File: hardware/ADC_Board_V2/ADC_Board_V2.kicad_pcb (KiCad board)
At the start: 2 copper layers, 11 parts, among them J1 Pot 01, J2 Pot 02, J3 Pot 03, J4 Pot 04, J5 Pot 05, J6 Pot 06, J7 Pot 07, J8 Pot 08, J9 Data, U1 MCP3008

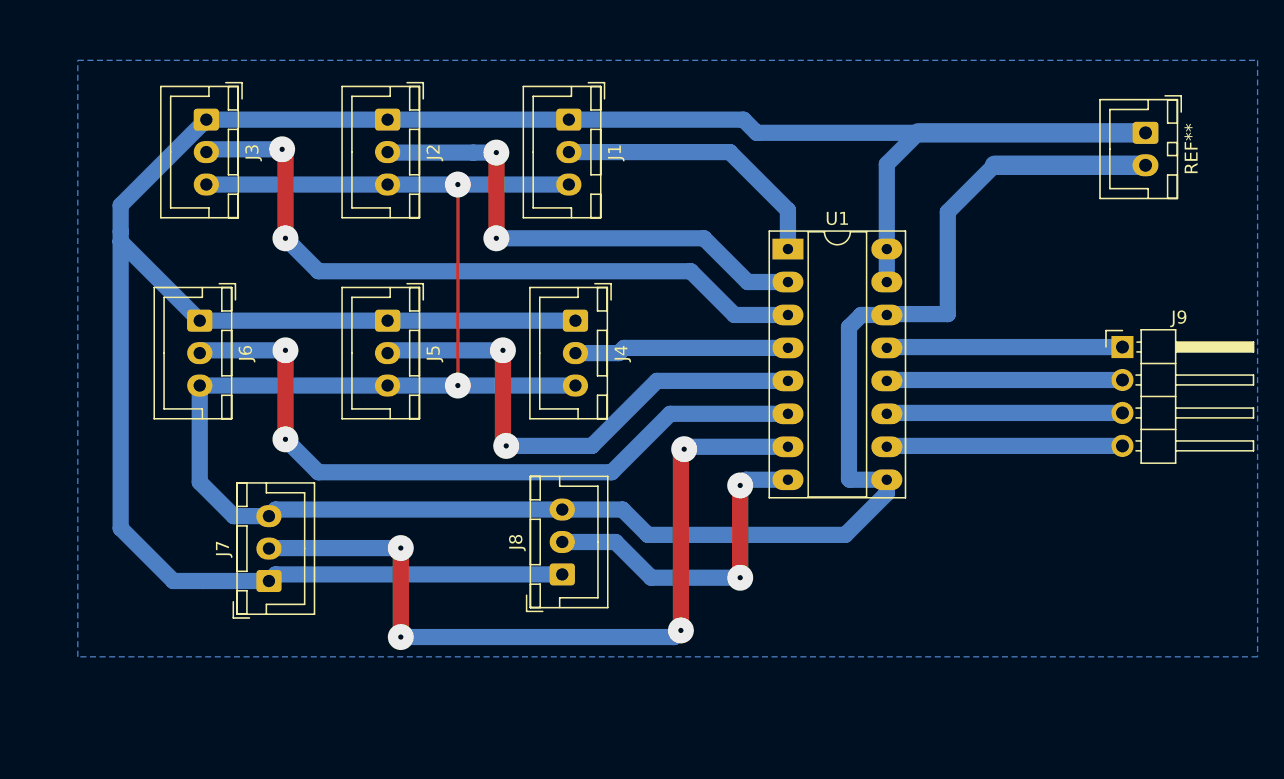
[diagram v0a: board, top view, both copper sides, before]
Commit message: updated ADC board design
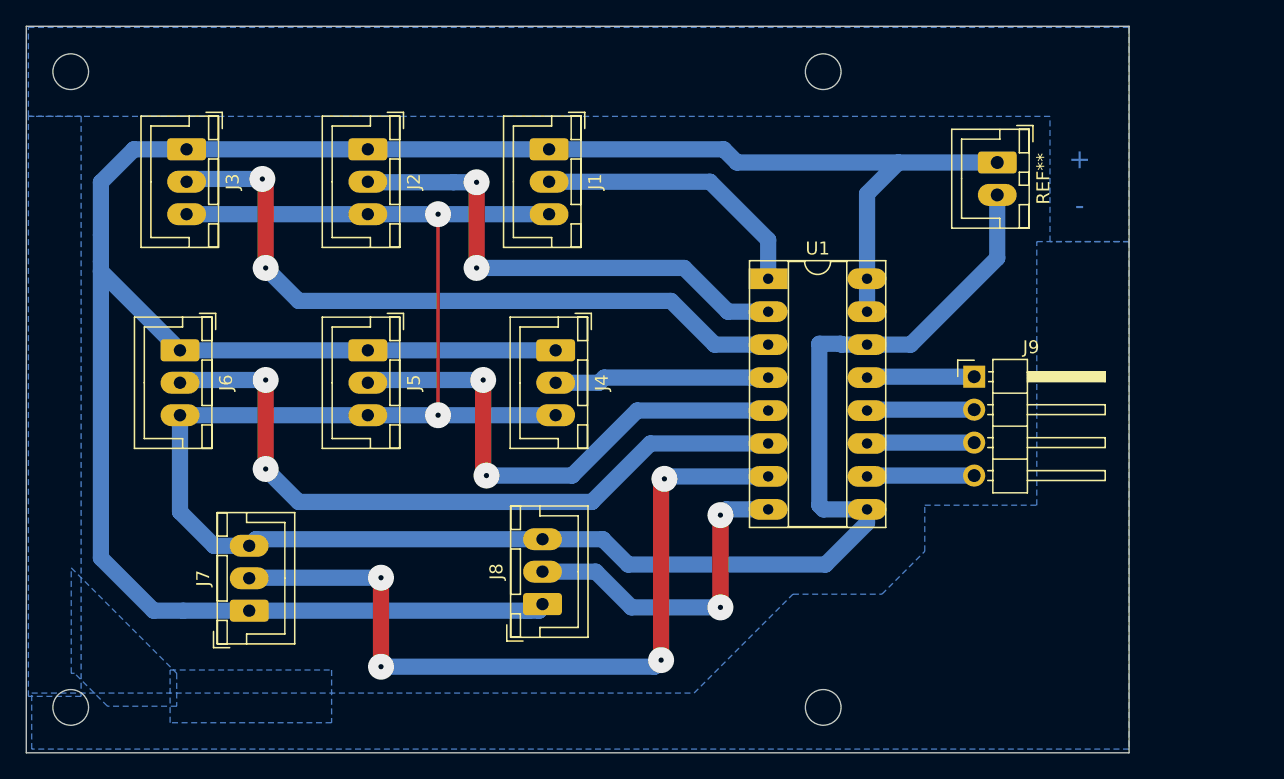
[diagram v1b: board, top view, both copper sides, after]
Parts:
- moved J9 11.7 mm to (135.6, 80.0)
- moved REF** 11.7 mm to (137.4, 63.5)
- moved J1 2.75 mm to (102.9, 62.5)
- moved J2 2.75 mm to (88.9, 62.5)
- moved J4 2.75 mm to (103.4, 78.0)
- moved J5 2.75 mm to (88.9, 78.0)
- moved J6 2.75 mm to (74.4, 78.0)
- moved J7 2.75 mm to (79.8, 98.0)
- moved J8 2.75 mm to (102.4, 97.5)
- moved U1 2.75 mm to (119.8, 72.5)
- moved J3 2.75 mm to (74.9, 62.5)
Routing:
- net Net-(J9-Pad4): track 18.2 -> 8.29 mm
- net Net-(J9-Pad3): track 18.2 -> 8.29 mm
- net Net-(J9-Pad2): track 18.2 -> 8.29 mm
- net Net-(J9-Pad1): track 18.2 -> 8.29 mm
- net GNDD: track 184.5 -> 175.0 mm
- net +3V3: track 193.0 -> 185.9 mm
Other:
- board outline added: 85 x 56 mm
- board text added: "+"
- board text added: "-"
